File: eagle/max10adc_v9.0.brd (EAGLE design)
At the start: 98 x 79 mm, 198 parts, among them IC1 MAX19506, IC2 MAX19506, J1 MOLEX_BNC_73100-0105, J2 MOLEX_BNC_73100-0105, J3 MOLEX_BNC_73100-0105, J4 MOLEX_BNC_73100-0105, K1 AQY21SOP, K2 AQY21SOP, K3 AQY21SOP, K4 AQY21SOP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

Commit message: v9.01
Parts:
- removed R10M_1, R10M_2, R10M_3, R10M_4: 10M, resistor:R0805
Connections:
- removed net N$27: R10M_2.2, S2.1
- removed net N$30: R10M_3.2, S3.1
- removed net N$33: R10M_4.2, S4.1
- removed net N10M_1: R10M_1.2, S1.1
- net GND: no longer R10M_1.1, R10M_2.1, R10M_3.1, R10M_4.1
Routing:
- net N$33: track 32.1 -> 0.00 mm, vias 1 -> 0
- net N10M_1: track 25.7 -> 0.00 mm
- net N$30: track 23.0 -> 0.00 mm
- net N$27: track 22.7 -> 0.00 mm, vias 1 -> 0
- net GND: track 234.7 -> 229.3 mm, vias 117 -> 114
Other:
- board text added: "Haasoscope v9.01"
- board text removed: "Haasoscope v9.0"

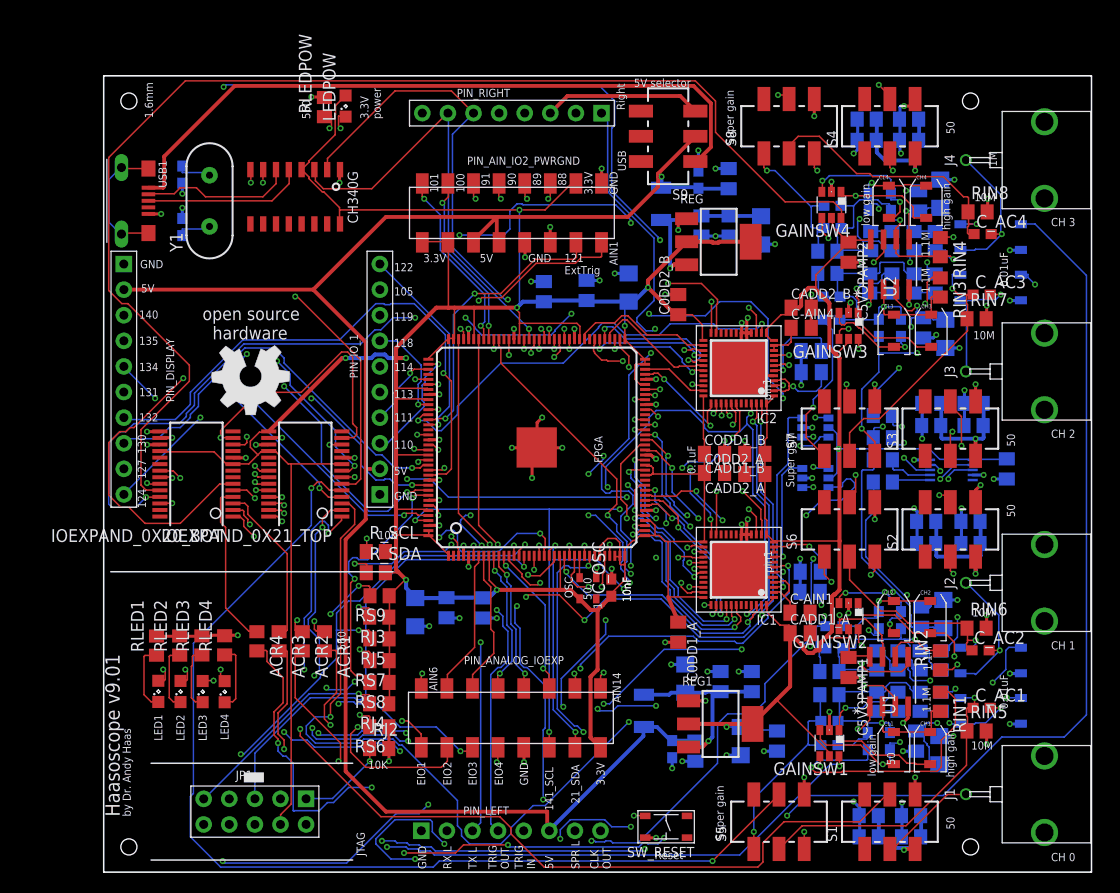
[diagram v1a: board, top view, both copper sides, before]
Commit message: better routing, using just 6mil distance between drills and traces
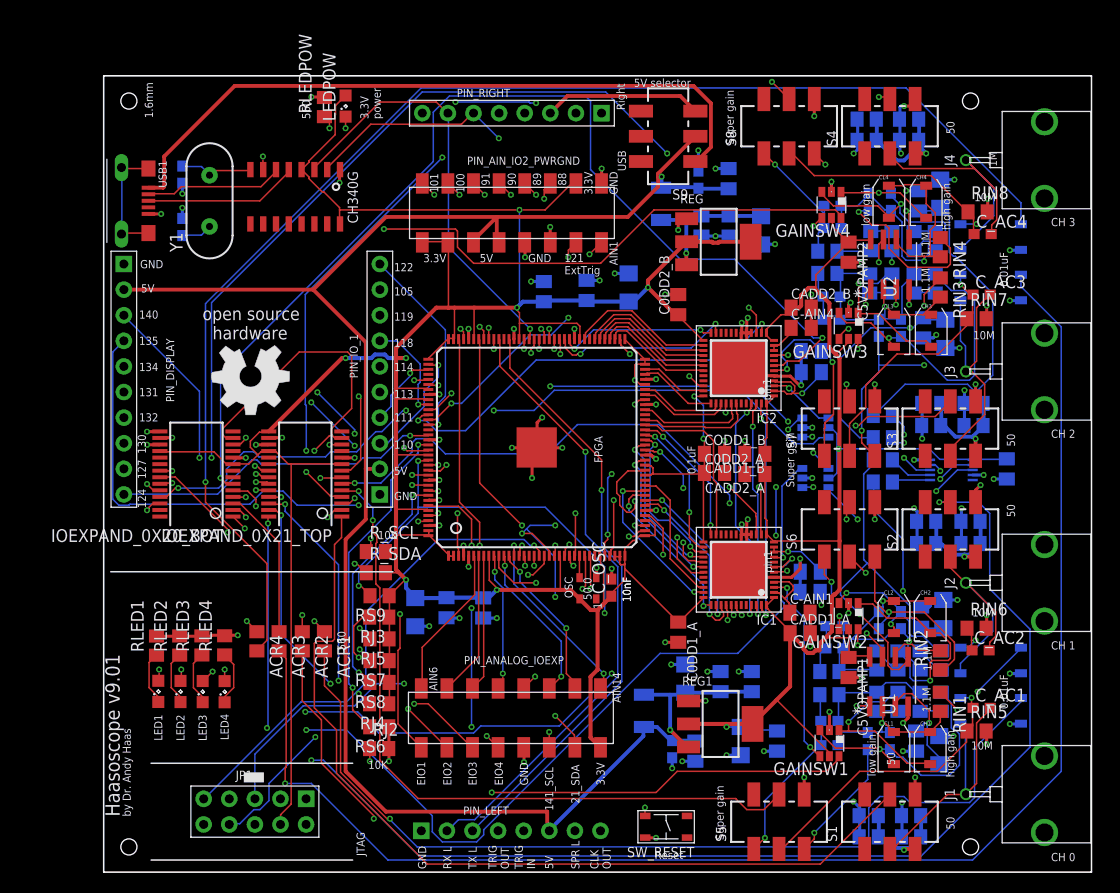
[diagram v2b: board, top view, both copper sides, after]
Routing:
- net E_21_B5: track 135.5 -> 60.5 mm, vias 2 -> 3
- net E_GSW2: track 152.3 -> 95.4 mm, vias 6 -> 4
- net E_21_B2: track 123.7 -> 72.9 mm, vias 3 -> 4
- net E_21_B6: track 70.9 -> 118.2 mm
- net E_21_B4: track 105.8 -> 71.6 mm
- net E_OVSAMP2: track 115.2 -> 148.2 mm, vias 6 -> 2
- net E_21_B1: track 105.2 -> 137.8 mm, vias 7 -> 3
- net E_OVSAMP1: track 103.7 -> 74.3 mm, vias 7 -> 3
- net N$35: track 161.7 -> 134.0 mm, vias 3 -> 1
- net E_GSW4: track 124.1 -> 98.7 mm, vias 0 -> 2
- net E_SHDN2: track 128.5 -> 105.7 mm, vias 4 -> 2
- net L132: track 55.1 -> 33.8 mm, vias 1 -> 3
- net D0A: track 34.7 -> 13.4 mm, vias 7 -> 0
- net +3V3: track 377.8 -> 398.3 mm, vias 8 -> 10
- net CLKINFROMRIGHT_26: track 65.5 -> 45.6 mm, vias 4 -> 1
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
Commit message: names on silkscreen
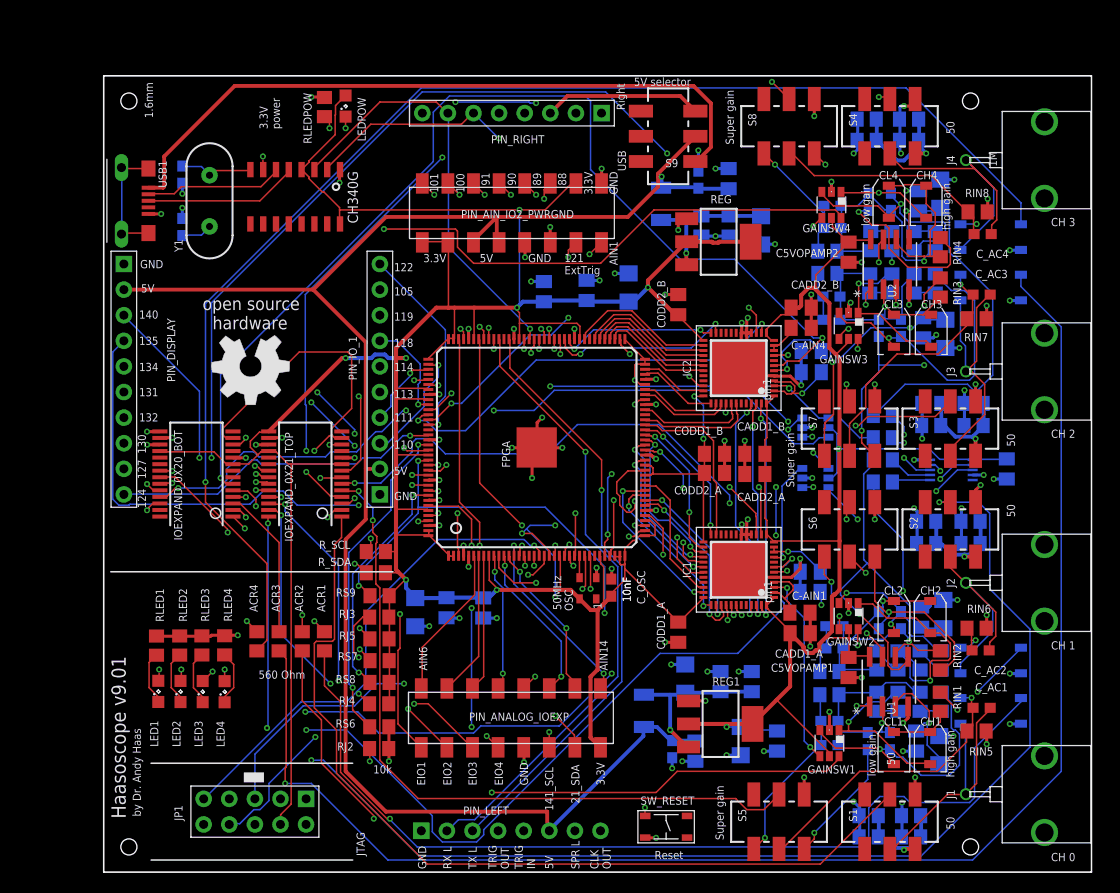
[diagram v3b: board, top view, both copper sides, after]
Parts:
- ROFFSET1: value 200R -> 200
- moved GOLD_ORB_SM1 1.00 mm to (2.60, 38.2)
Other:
- board text added: "10k"
- board text added: "50MHz"
- board text added: "560 Ohm"
- board text removed: "50.0"
- board text removed: "560"
